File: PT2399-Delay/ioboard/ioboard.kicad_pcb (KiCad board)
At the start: 2 copper layers, 19 x 108 mm, 13 parts, among them J2 Conn_02x05_Odd_Even

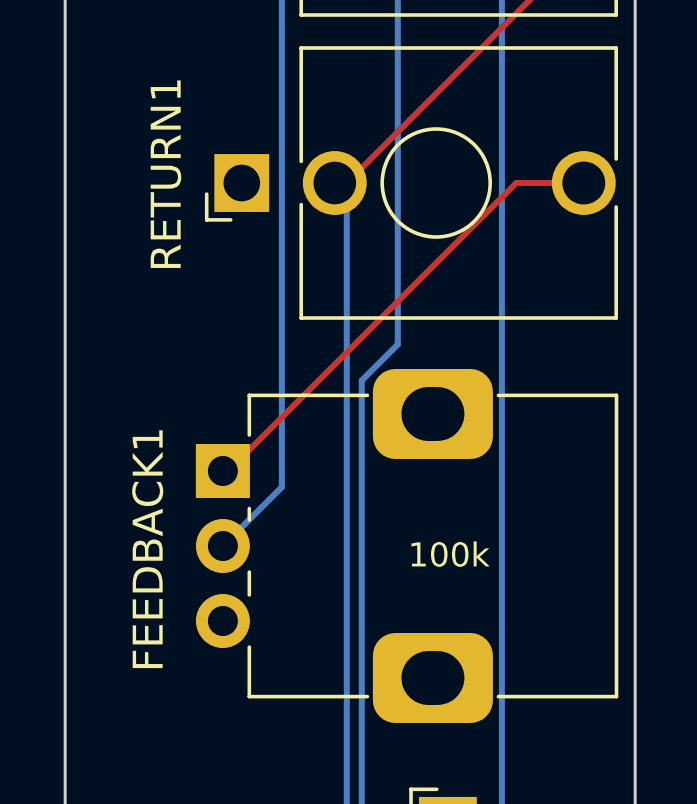
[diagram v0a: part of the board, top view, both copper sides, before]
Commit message: Fixed feedback orientation (pin 1 should point low)
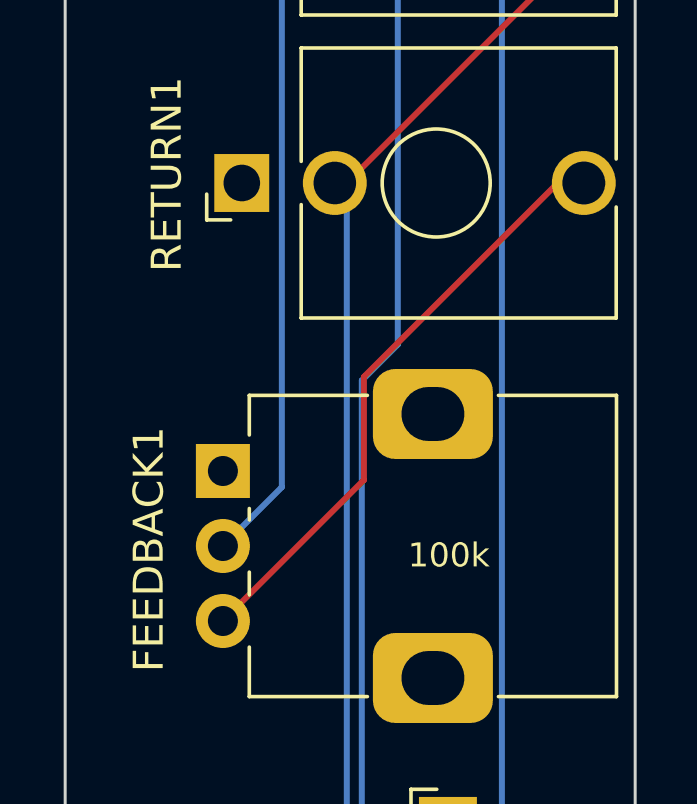
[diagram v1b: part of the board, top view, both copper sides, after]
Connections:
- FEEDBACK1 pad 1: Net-(FEEDBACK1-Pad1) -> GND
- FEEDBACK1 pad 3: GND -> Net-(FEEDBACK1-Pad3)
- RETURN1 pad T: Net-(FEEDBACK1-Pad1) -> Net-(FEEDBACK1-Pad3)
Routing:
- net Net-(FEEDBACK1-Pad3): track 0.00 -> 20.1 mm
- net Net-(FEEDBACK1-Pad1): track 16.4 -> 0.00 mm
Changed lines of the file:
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@@
 	(net 10 "unconnected-(MIX1-PadTN)")
 	(net 11 "unconnected-(WET1-PadTN)")
-	(net 12 "Net-(FEEDBACK1-Pad1)")
+	(net 12 "Net-(FEEDBACK1-Pad3)")
 	(net 13 "+5V")
 	(net 14 "Net-(R2-Pad1)")
@@
 			(layers "*.Cu" "*.Mask")
 			(remove_unused_layers no)
-			(net 12 "Net-(FEEDBACK1-Pad1)")
+			(net 12 "Net-(FEEDBACK1-Pad3)")
 			(pintype "passive")
 		)
@@
 			(layers "*.Cu" "*.Mask")
 			(remove_unused_layers no)
-			(net 12 "Net-(FEEDBACK1-Pad1)")
+			(net 8 "GND")
 			(pinfunction "1")
 			(pintype "passive")
@@
 			(layers "*.Cu" "*.Mask")
 			(remove_unused_layers no)
-			(net 8 "GND")
+			(net 12 "Net-(FEEDBACK1-Pad3)")
 			(pinfunction "3")
 			(pintype "passive")
@@
 	)
 	(segment
+		(start 123.949895 112.69)
+		(end 123.77 112.69)
+		(width 0.2)
+		(layer "F.Cu")
+		(net 8)
+	)
+	(segment
 		(start 125.07 66.37)
 		(end 124.4 65.7)
@@
 	)
 	(segment
-		(start 133.549895 103.09)
-		(end 123.949895 112.69)
+		(start 128.47 112.99)
+		(end 128.47 109.55)
 		(width 0.2)
 		(layer "F.Cu")
@@
 	)
 	(segment
-		(start 123.949895 112.69)
-		(end 123.77 112.69)
+		(start 134.93 103.09)
+		(end 135.8 103.09)
+		(width 0.2)
+		(layer "F.Cu")
+		(net 12)
+	)
+	(segment
+		(start 128.47 109.55)
+		(end 134.93 103.09)
 		(width 0.2)
 		(layer "F.Cu")
@@
 	)
 	(segment
-		(start 136.2 103.09)
-		(end 133.549895 103.09)
+		(start 123.77 117.69)
+		(end 128.47 112.99)
 		(width 0.2)
 		(layer "F.Cu")

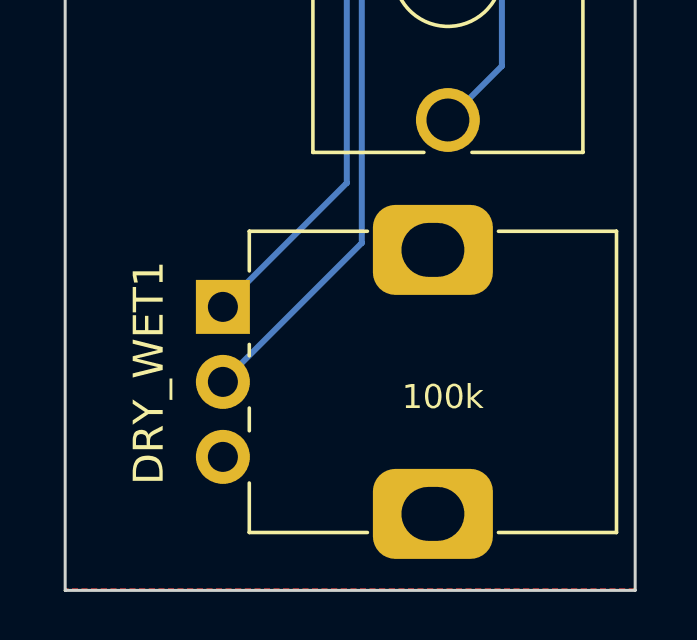
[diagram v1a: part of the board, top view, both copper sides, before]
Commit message: Fixed up pinout of dry/wet as well
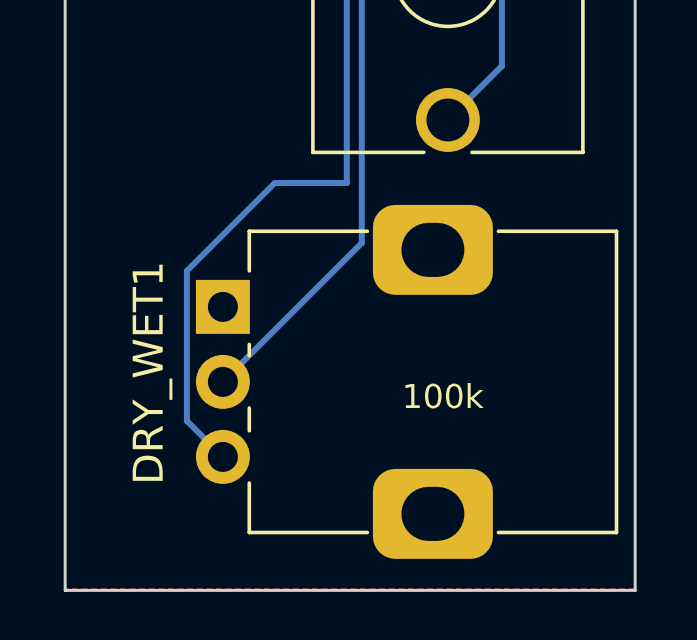
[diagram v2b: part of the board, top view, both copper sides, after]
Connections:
- DRY_WET1 pad 1: /BUFFERED_WET -> GND
- DRY_WET1 pad 3: GND -> /BUFFERED_WET
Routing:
- net /BUFFERED_WET: track 113.3 -> 120.7 mm
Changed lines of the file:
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@@
 			(layers "*.Cu" "*.Mask")
 			(remove_unused_layers no)
-			(net 5 "/BUFFERED_WET")
+			(net 8 "GND")
 			(pinfunction "1")
 			(pintype "passive")
@@
 			(layers "*.Cu" "*.Mask")
 			(remove_unused_layers no)
-			(net 8 "GND")
+			(net 5 "/BUFFERED_WET")
 			(pinfunction "3")
 			(pintype "passive")
@@
 	)
 	(segment
+		(start 122.57 140.9)
+		(end 122.57 145.9)
+		(width 0.2)
+		(layer "B.Cu")
+		(net 5)
+	)
+	(segment
 		(start 134.435 54.974598)
 		(end 134.435 91.625)
@@
 	)
 	(segment
+		(start 125.5 137.97)
+		(end 122.57 140.9)
+		(width 0.2)
+		(layer "B.Cu")
+		(net 5)
+	)
+	(segment
+		(start 122.57 145.9)
+		(end 123.77 147.1)
+		(width 0.2)
+		(layer "B.Cu")
+		(net 5)
+	)
+	(segment
 		(start 134.3 44.2)
 		(end 127.2925 44.2)
@@
 	)
 	(segment
-		(start 123.77 142.1)
-		(end 127.9 137.97)
-		(width 0.2)
-		(layer "B.Cu")
+		(start 127.9 137.97)
+		(end 125.5 137.97)
+		(width 0.2)
+		(layer "B.Cu")
